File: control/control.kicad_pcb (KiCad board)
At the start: 2 copper layers, 54.9 x 56.9 mm, 62 parts, among them J1 Conn_01x02_Pin, J2 Conn_01x04_Male, J3 Conn_01x02_Pin, P1 Conn_01x03_Pin, P2 Conn_01x03_Pin, P3 Conn_01x03_Pin, P4 Conn_01x03_Pin, SW2 SW_Push, U1 STM32F103C8Tx, Y1 8Mhz

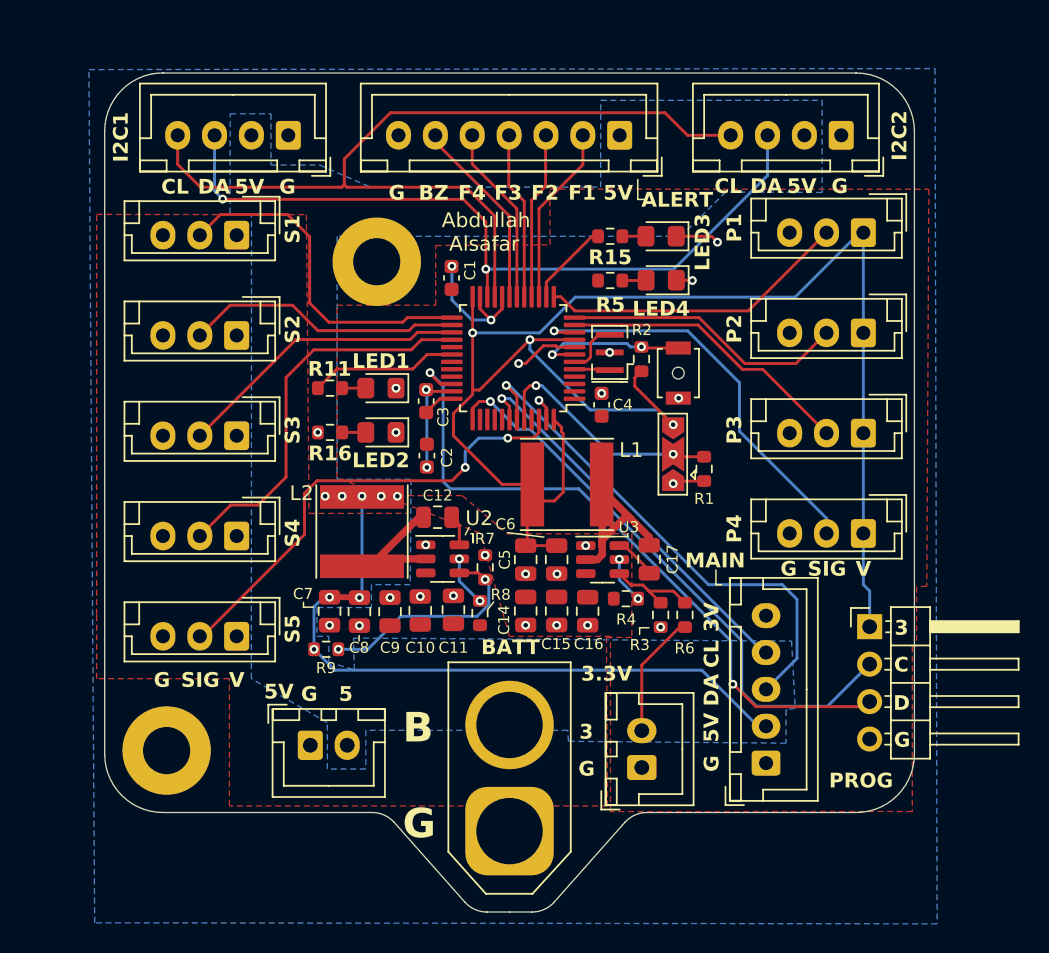
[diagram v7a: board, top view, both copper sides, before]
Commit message: updated programmer & battery footprints
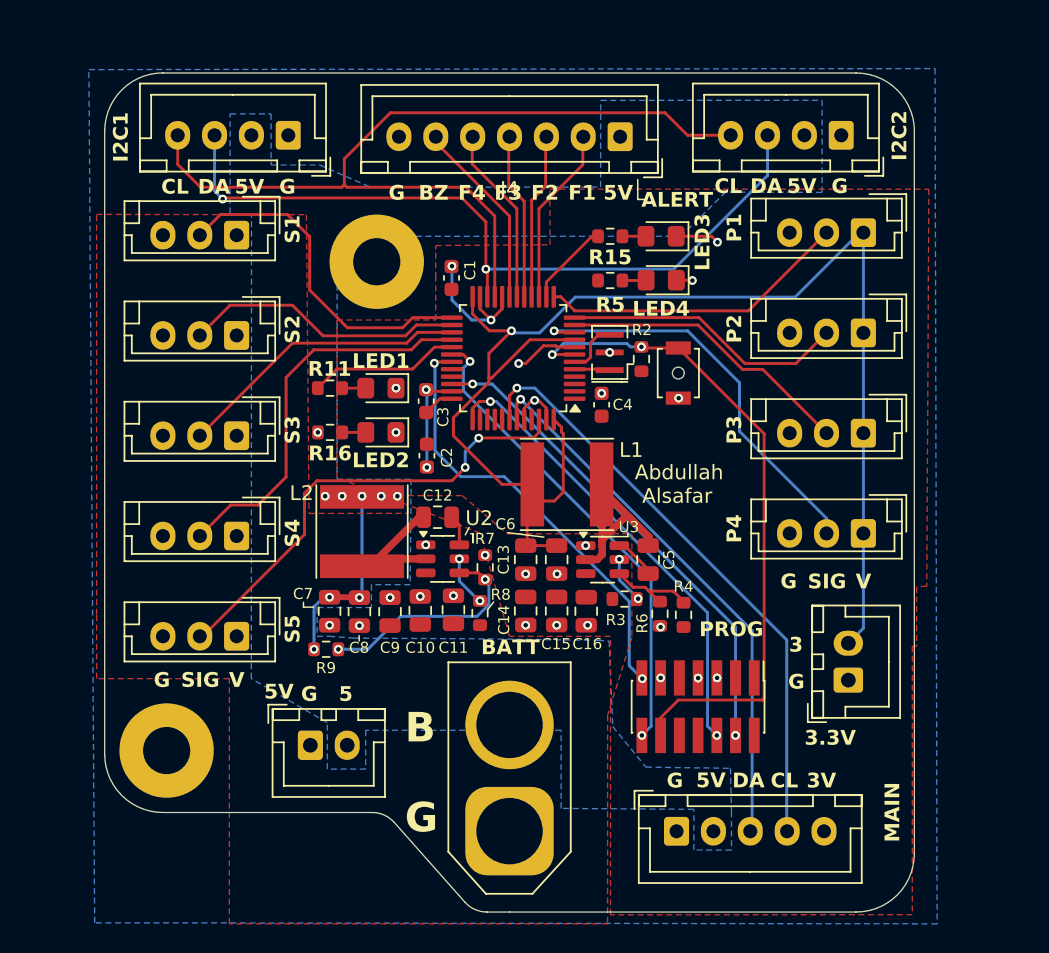
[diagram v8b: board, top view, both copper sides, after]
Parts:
- removed ALERT: Conn_01x07_Pin, Connector_JST:JST_XH_B7B-XH-A_1x07_P2.50mm_Vertical
- removed C17: 0.1uF, Capacitor_SMD:C_0805_2012Metric
- removed H** (x2): MountingHole_3.2mm_M3, MountingHole:MountingHole_3.2mm_M3
- removed J2: Conn_01x04_Male, Connector_PinHeader_2.54mm:PinHeader_1x04_P2.54mm_Horizontal
- removed JP1: Jumper_3_Open, Jumper:SolderJumper-3_P2.0mm_Open_TrianglePad1.0x1.5mm
- removed R1: 10k, Resistor_SMD:R_0603_1608Metric
- removed the REF** at (132.8, 73.7)
- added C13: 22uF, Capacitor_SMD:C_0805_2012Metric, F.Cu at (141.7, 87.3)
- added J4: Conn_01x07_Pin, Connector_JST:JST_XH_B7B-XH-A_1x07_P2.50mm_Vertical, F.Cu at (148.1, 58.6)
- added J5: Conn_ST_STDC14, Connector_PinHeader_1.27mm:PinHeader_2x07_P1.27mm_Vertical_SMD, F.Cu at (153.4, 97.3)
- added REF**: MountingHole_3.2mm_M3_Pad, MountingHole:MountingHole_3.2mm_M3_Pad, F.Cu at (117.3, 100.2)
- added REF**: MountingHole_3.2mm_M3_Pad, MountingHole:MountingHole_3.2mm_M3_Pad, F.Cu at (131.6, 67.1)
- C5: value 22uF -> 0.1uF
- R4: value 10k -> 33.2k
- R6: value 33.2k -> 10k
- moved J1 15.2 mm to (163.6, 95.5)
- moved C5 8.31 mm to (150.0, 87.3), turned to -90 degrees
- moved ISC3 7.63 mm to (151.9, 105.7), turned to 0 degrees
- moved R4 4.06 mm to (152.4, 91.0), turned to 90 degrees
- moved R3 2.67 mm to (148.4, 90.0), turned to 180 degrees
- moved R6 1.70 mm to (150.8, 91.0)
- moved G*** 0.43 mm to (147.1, 68.2)
- moved C16 0.09 mm to (145.8, 90.8)
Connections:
- net Net-(U1-NRST) renamed /~{RST}
- C5 pad 1: GND -> Net-(U3-SW)
- C5 pad 2: +3.3V -> Net-(U3-VBST)
- R3 pad 1: GND -> Net-(U3-EN)
- R3 pad 2: Net-(U3-VFB) -> +BATT
- R4 pad 1: Net-(U3-EN) -> +3.3V
- R4 pad 2: +BATT -> Net-(U3-VFB)
- R6 pad 1: +3.3V -> GND
- U1 pad 29: unconnected-(U1-PA8-Pad29) -> LED1
- U1 pad 30: LED1 -> TX1
- U1 pad 31: unconnected-(U1-PA10-Pad31) -> RX1
- U1 pad 44: Net-(JP1-C) -> GND
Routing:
- net /~{RST}: track 10.5 -> 45.4 mm
- net +5V: track 48.6 -> 15.2 mm
- net TX1: track 0.00 -> 32.5 mm, vias 0 -> 2
- net RX1: track 0.00 -> 30.2 mm, vias 0 -> 2
- net +3.3V: track 125.0 -> 99.3 mm, vias 3 -> 1
- net Net-(JP1-C): track 16.3 -> 0.00 mm, vias 2 -> 0
- net SCL_{TOMAIN}: track 26.7 -> 40.7 mm
- net /SWDIO: track 46.6 -> 33.4 mm
- net /SWCLK: track 39.6 -> 31.4 mm, vias 1 -> 2
- net SDA_{TOMAIN}: track 35.3 -> 37.3 mm
- net GND: track 28.3 -> 28.1 mm, vias 28 -> 30
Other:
- outline, holes or cut-outs redrawn
- board text removed: "C"
- board text removed: "D"
